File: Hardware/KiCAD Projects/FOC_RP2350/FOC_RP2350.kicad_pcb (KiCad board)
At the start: 4 copper layers, 72.5 x 39.7 mm, 67 parts, among them J401 GT-USB-7025, J402 DB125-2.54-6P-GN-S, J403 MKS Power, J404 XT30U-M, J405 ZX-PZ2.54-2-6PZZ, J406 PZ254-1-13-Z-8.5, J407 PZ254-1-13-Z-8.5, Q401 AO3401A, SW201 KMS231GLFS, SW202 KMS231GLFS, SW301 DSHP04TSGER, U201 RP2354B, U301 THVD1424RGTR, U401 AMS1117-3.3, U402 ACS711KLCTR-25AB-T, U403 TSR1-2450E, U404 TSR1-2433E, Y201 ABM8-272-T3

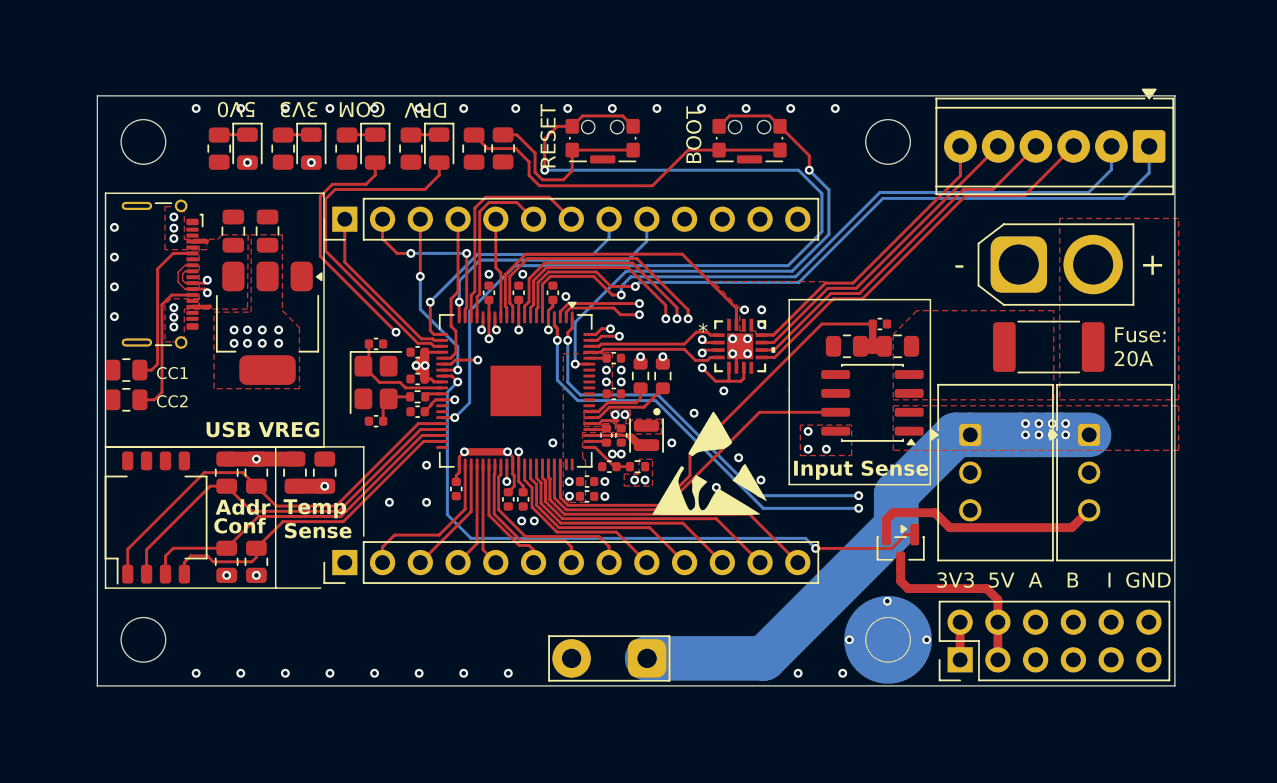
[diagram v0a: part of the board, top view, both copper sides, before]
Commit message: Hardware update
- Removed 5V net as it is not really needed for typical SimpleFOC encoders. This reduces part cost a lot.
- Fixed SPI pin assignment
- Exposed another GPIO pin in place of the +5V pin
- Boards changed to transfer power via the standoff pads instead of a solder connection
- Moved accelerometer to the controller board
- Resistance changes to reduce BOM
- Replaced encoder connection with JST-XH
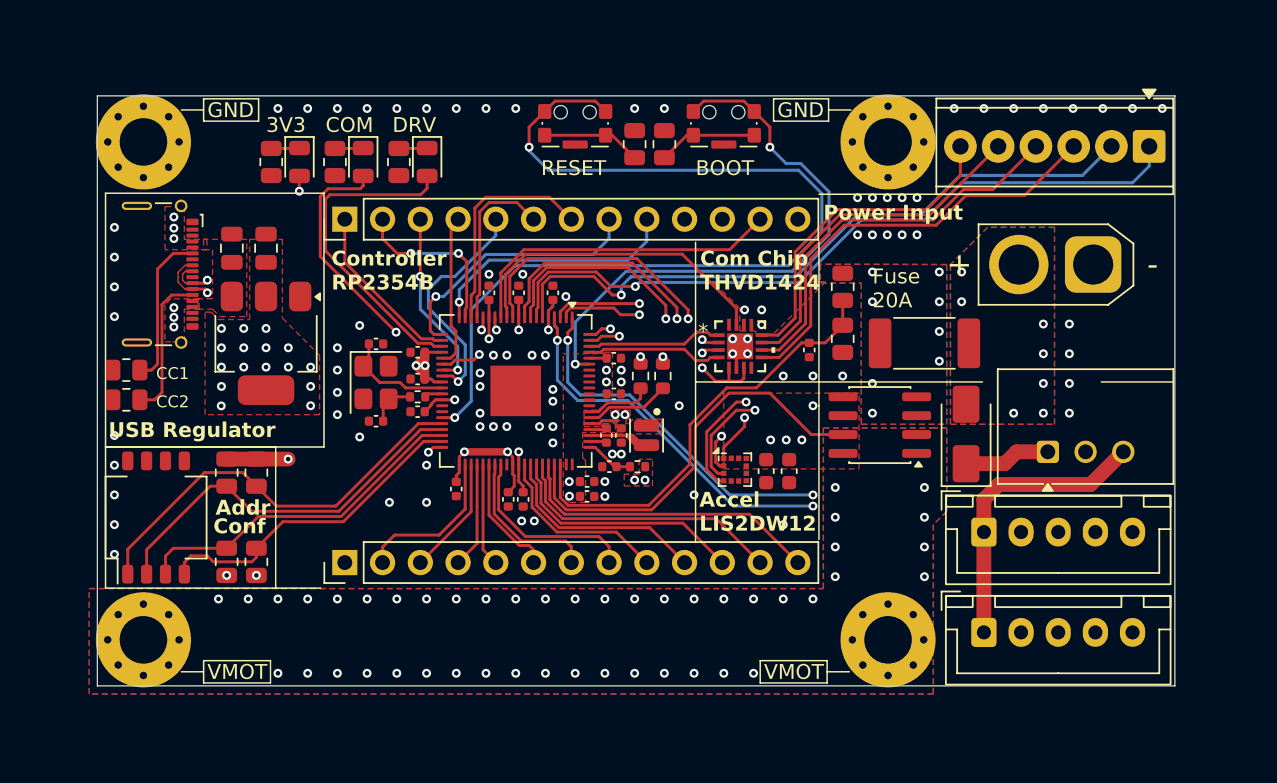
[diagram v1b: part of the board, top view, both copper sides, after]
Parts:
- removed D402: KT-0805G, LED_SMD:LED_0805_2012Metric
- removed the G*** at (163.3, 105.0)
- removed J405: ZX-PZ2.54-2-6PZZ, Connector_PinHeader_2.54mm:PinHeader_2x06_P2.54mm_Vertical
- removed Q401: AO3401A, Package_TO_SOT_SMD:SOT-23
- removed R405: 1k, Resistor_SMD:R_0805_2012Metric
- removed R406: 680, Resistor_SMD:R_0805_2012Metric
- removed TH301: NTCS0805E3103JMT, Resistor_SMD:R_0805_2012Metric
- removed U404: TSR1-2433E, Converter_DCDC:Converter_DCDC_TRACO_TSR1-xxxxE_THT
- added C301: 1u, Capacitor_SMD:C_0603_1608Metric, F.Cu at (168.4, 105.4)
- added C302: 1u, Capacitor_SMD:C_0603_1608Metric, F.Cu at (166.8, 105.4)
- added D303: KT-0805G, LED_SMD:LED_0805_2012Metric, F.Cu at (135.4, 84.6)
- added H401: MountingHole_Pad, MountingHole:MountingHole_3.2mm_M3_Pad_Via, F.Cu at (175.1, 116.8)
- added H402: MountingHole_Pad, MountingHole:MountingHole_3.2mm_M3_Pad_Via, F.Cu at (125.0, 116.8)
- added H403: MountingHole_Pad, MountingHole:MountingHole_3.2mm_M3_Pad_Via, F.Cu at (125.0, 83.2)
- added H404: MountingHole_Pad, MountingHole:MountingHole_3.2mm_M3_Pad_Via, F.Cu at (175.1, 83.2)
- added J408: Conn_01x05, Connector_JST:JST_XH_B5B-XH-A_1x05_P2.50mm_Vertical, F.Cu at (181.5, 109.5)
- added U302: LIS2DE12, Package_LGA:LGA-12_2x2mm_P0.5mm, F.Cu at (164.8, 105.3)
- D401: value KT-0805G -> SS12; footprint LED_SMD:LED_0805_2012Metric -> Diode_SMD:D_SMA
- J403: value MKS Power -> Conn_01x05; footprint TestPoint:TestPoint_2Pads_Pitch5.08mm_Drill1.3mm -> Connector_JST:JST_XH_B5B-XH-A_1x05_P2.50mm_Vertical
- R301: value 4.7k -> 1k
- R302, R303: value 680 -> 1k
- R304, R305, R306, R307: value 4.7k -> 5.1k
- U403: value TSR1-2450E -> TSR1-2433E
- moved D401 52.0 mm to (180.3, 102.9), turned to 90 degrees
- moved J403 22.7 mm to (181.5, 116.2), turned to 0 degrees
- moved R301 21.0 mm to (133.6, 84.6), turned to 90 degrees
- moved R205 12.8 mm to (160.0, 83.4), turned to -90 degrees
- moved R202 8.85 mm to (158.0, 83.4), turned to -90 degrees
- moved F401 8.37 mm to (177.5, 96.8)
- moved R403 5.46 mm to (172.0, 93.0), turned to 90 degrees
- moved C403 5.06 mm to (169.8, 97.2), turned to -90 degrees
- moved J404 5.00 mm to (188.9, 91.5), turned to 180 degrees
- moved U403 3.01 mm to (185.8, 104.1), turned to 90 degrees
- moved SW201 2.10 mm to (154.0, 82.0)
- moved SW202 2.00 mm to (164.0, 82.0)
- moved U402 1.58 mm to (174.5, 102.3)
- moved U401 1.35 mm to (133.2, 96.8)
- moved D301 1.21 mm to (144.0, 84.6)
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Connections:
- D401 pad 2: /Power and Connections/5V -> /Power and Connections/VCON
- J403 pad 1: /Power and Connections/VMOT -> /Comms/3V3
- J403 pad 2: GND -> /I2C1_SDA
- J406 pad 12: /Power and Connections/5V -> /Controller/GPIO14
- R301 pad 1: /Comms/3V3 -> GND
- R301 pad 2: /Comms/Board Temp -> Net-(D303-K)
- U201 pad 13: /SPI1_TX -> /Controller/GPIO14
- U201 pad 28: /Controller/GPIO27 -> /SPI1_TX
- U201 pad 40: /Controller/GPIO32 -> /Comms/Accel_CS
- U201 pad 49: /Comms/Board Temp -> /Controller/ADC0
- U402 pad 1: /Power and Connections/VMOT -> VMOT
- U402 pad 2: /Power and Connections/VMOT -> VMOT
- U403 pad 1: /Power and Connections/VMOT -> Net-(D401-K)
- U403 pad 3: Net-(Q401-S) -> /Comms/3V3
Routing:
- net /Power and Connections/5V: track 88.7 -> 0.00 mm, vias 1 -> 0
- net /Controller/GPIO27: track 43.2 -> 0.00 mm, vias 2 -> 0
- net /SPI1_TX: track 6.74 -> 48.6 mm, vias 0 -> 2
- net /Power and Connections/VMOT: track 37.2 -> 0.00 mm, vias 8 -> 0
- net /SPI1_RX: track 10.4 -> 45.8 mm, vias 0 -> 1
- net /SPI1_SCK: track 12.2 -> 46.2 mm, vias 2 -> 3
- net /Comms/Accel_CS: track 0.00 -> 24.6 mm, vias 0 -> 2
- net /Controller/GPIO14: track 0.00 -> 21.9 mm
- net Net-(R205-Pad2): track 23.5 -> 6.68 mm
- net Net-(Q401-S): track 15.7 -> 0.00 mm
- net /Comms/Board Temp: track 15.5 -> 0.00 mm, vias 2 -> 0
- net /Comms/3V3: track 37.4 -> 47.3 mm, vias 30 -> 38
- net Net-(R202-Pad2): track 12.4 -> 6.68 mm
- net /I2C1_SDA: track 45.0 -> 39.5 mm
- net /I2C0_SDA: track 43.1 -> 38.8 mm
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- added copper zone on B.Cu, net /Power and Connections/VCON
- added copper zone on B.Cu, net /Power and Connections/VIN
- added copper zone on B.Cu, net VMOT
- added copper zone on F.Cu, net VMOT
- removed copper zone on F.Cu, net /Power and Connections/VMOT
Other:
- outline, holes or cut-outs redrawn
- board text added: "Accel LIS2DW12"
- board text added: "Com Chip THVD1424"
- board text added: "Controller RP2354B"
- board text added: "Encoder GPIO Assignment GND 7 5 6 3V3 (I2C0) GND 4 3 2 3V3(I2C1/SPI0)"
- board text added: "Fuse 20A"
- board text added: "GPIO27"
- board text added: "Power Input"
- board text added: "USB Regulator"
- board text added: "Voltage Limits: TSR 1: 6.5-36V TSR 0.6WI: 9.0-72V MKS Drive: 12-24V DRV8323: 6-60V"
- board text removed: "3.3V"
- board text removed: "5V"
- board text removed: "5V0"
- board text removed: "A"
- board text removed: "B"
- board text removed: "Encoder GPIO Assignment GND 7 5 6 5V (I2C0) GND 4 3 2 5V (I2C1/SPI0)"
- board text removed: "Fuse: 20A"
- board text removed: "I"
- board text removed: "Input Sense"
- board text removed: "POWER CONVERTER"
- board text removed: "SHIELD"
- board text removed: "Temp Sense"
- board text removed: "USB VREG"
- board text removed: "Voltage Limits: TSR 1: 6.5-36V TSR 0.6WI: 9.0-72V MKS Drive: 12-24V"

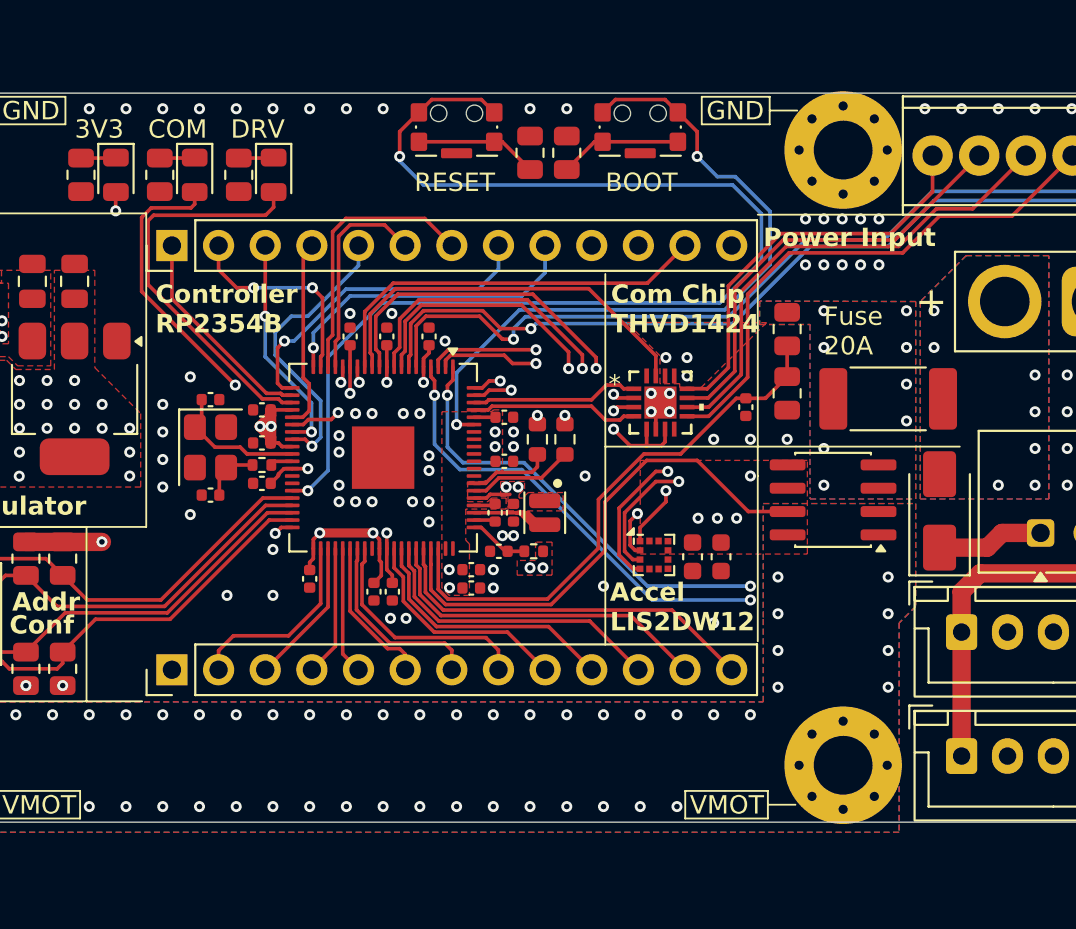
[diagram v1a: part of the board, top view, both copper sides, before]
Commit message: Driver redesign to allow 8323H and 8323S
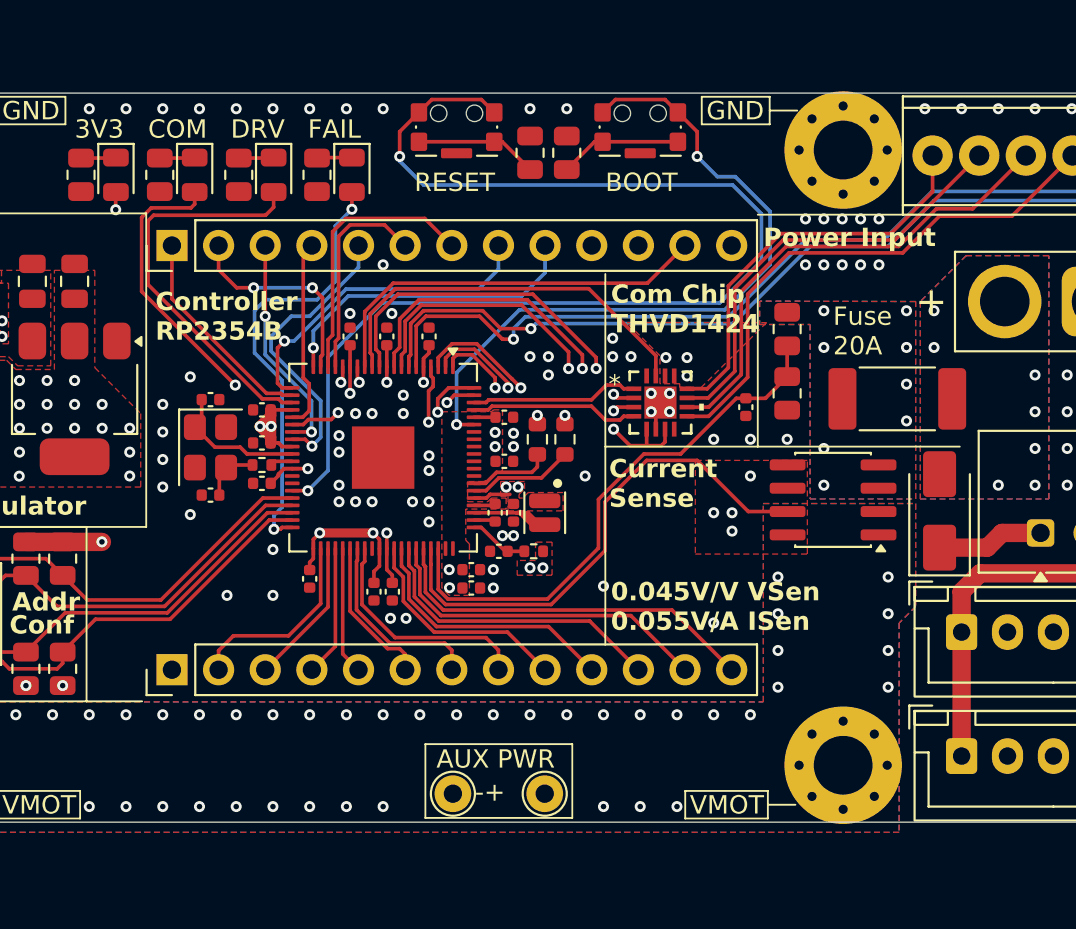
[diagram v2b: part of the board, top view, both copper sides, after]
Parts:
- removed C301, C302: 1u, Capacitor_SMD:C_0603_1608Metric
- removed G***: LOGO, LOGO
- removed U302: LIS2DE12, Package_LGA:LGA-12_2x2mm_P0.5mm
- added D304: KT-0805R, LED_SMD:LED_0805_2012Metric, F.Cu at (148.3, 84.6)
- added H405: MountingHole_Pad, TestPoint:TestPoint_THTPad_D2.0mm_Drill1.0mm, F.Cu at (158.8, 118.3)
- added H406: MountingHole_Pad, TestPoint:TestPoint_THTPad_D2.0mm_Drill1.0mm, F.Cu at (153.8, 118.3)
- added R308: 1k, Resistor_SMD:R_0805_2012Metric, F.Cu at (146.4, 84.6)
- moved F401 0.50 mm to (178.0, 96.8)
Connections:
- net /ADC1 renamed /GPIO41_ADC1
- net /ADC2 renamed /GPIO42_ADC2
- net /ADC3 renamed /GPIO43_ADC3
- net /ADC4 renamed /GPIO44_ADC4
- net /ADC5 renamed /GPIO45_ADC5
- net /ADC6 renamed /GPIO46_ADC6
- net /ADC7 renamed /GPIO47_ADC7
- net /Comms/ComBus_Rxen renamed /GPIO12_RXEN
- net /Comms/ComBus_Term renamed /GPIO10_TERM
- net /Comms/ComBus_Txen renamed /GPIO11_TXEN
- net /I2C0_SCL renamed /GPIO5_I2C0_SCL
- net /I2C1_SCL renamed /GPIO3_I2C1_SCL
- net /I2C1_SDA renamed /GPIO2_I2C1_SDA
- net /PWM10A renamed /GPIO36_PWM10A
- net /PWM10B renamed /GPIO37_PWM10B
- net /PWM11A renamed /GPIO38_PWM11A
- net /PWM11B renamed /GPIO39_PWM11B
- net /PWM8B renamed /GPIO33_PWM8B
- net /PWM9A renamed /GPIO34_PWM9A
- net /PWM9B renamed /GPIO35_PWM9B
- net /SPI1_RX renamed /GPIO24_SPI1_MISO
- net /SPI1_SCK renamed /GPIO26_SPI1_SCK
- net /SPI1_TX renamed /GPIO27_SPI1_MOSI
- net /UART0_RX renamed /GPIO1_UART0_RX
- net /UART0_TX renamed /GPIO0_UART0_TX
- net /UART1_RX_External renamed /GPIO9_UART1_RX
- net /UART1_RX_Shield renamed /GPIO21_UART1_RX
- net /UART1_TX_External renamed /GPIO8_UART1_TX
- net /UART1_TX_Shield renamed /GPIO20_UART1_TX
- J408 pad 2: /I2C0_SDA -> /GPIO4_I2C0_SDA
- J408 pad 4: /Controller/GPIO4 -> /Controller/GPIO6
- U201 pad 1: /Controller/GPIO4 -> /GPIO4_I2C0_SDA
- U201 pad 3: /I2C0_SDA -> /Controller/GPIO6
- U201 pad 40: /Comms/Accel_CS -> /Comms/Led3
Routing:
- net /Controller/GPIO4: track 45.7 -> 0.00 mm, vias 2 -> 0
- net /Controller/GPIO6: track 0.00 -> 44.8 mm, vias 0 -> 1
- net /GPIO4_I2C0_SDA: track 0.00 -> 40.1 mm, vias 0 -> 1
- net /I2C0_SDA: track 38.8 -> 0.00 mm, vias 1 -> 0
- net /GPIO24_SPI1_MISO: track 45.8 -> 10.4 mm, vias 1 -> 0
- net /GPIO26_SPI1_SCK: track 46.2 -> 12.2 mm, vias 3 -> 2
- net /GPIO27_SPI1_MOSI: track 48.6 -> 16.0 mm, vias 2 -> 1
- net /Comms/Accel_CS: track 24.6 -> 0.00 mm, vias 2 -> 0
- net /Comms/Led3: track 0.00 -> 24.0 mm, vias 0 -> 2
- net /GPIO2_I2C1_SDA: track 39.5 -> 47.5 mm
- net /GPIO3_I2C1_SCL: track 44.5 -> 51.5 mm
- net /Controller/GPIO7: track 47.5 -> 54.3 mm, vias 2 -> 1
- net Net-(D304-K): track 0.00 -> 1.91 mm
- net VMOT: vias 46 -> 41
- net GND: vias 88 -> 94
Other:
- board text added: "-+"
- board text added: "0.045V/V VSen 0.055V/A ISen"
- board text added: "A/SDA"
- board text added: "AUX PWR"
- board text added: "B/SCL"
- board text added: "Current Sense"
- board text added: "FAIL"
- board text added: "GPIO38"
- board text added: "GPIO41"
- board text added: "SPI1 MISO"
- board text added: "SPI1 MOSI"
- board text added: "SPI1 SCLK"
- board text added: "UART1 RX"
- board text added: "UART1 TX"
- board text added: "Z"
- board text removed: "Accel LIS2DW12"
- board text removed: "Encoder GPIO Assignment GND 7 5 6 3V3 (I2C0) GND 4 3 2 3V3(I2C1/SPI0)"
- board text removed: "IDX"
- board text removed: "IO38"
- board text removed: "IO41"
- board text removed: "MCU: RP2354B RS485: THVD1424 Xtal: 12MHZ"
- board text removed: "SCL"
- board text removed: "SDA"
- board text removed: "SPI1 RX"
- board text removed: "SPI1 SCK"
- board text removed: "SPI1 TX"
- board text removed: "U1 RX"
- board text removed: "U1 TX"
